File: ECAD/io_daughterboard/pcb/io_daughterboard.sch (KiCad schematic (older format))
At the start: 33 parts, among them P1 CONN_02X32, P2 CONN_02X32

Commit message: Annotated P2 pins.
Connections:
- net labels added: BTN_USER, BTN_~RESET, LCD_B5, LCD_DE, LCD_G2, LCD_G4, LCD_G5, LCD_PWM, LCD_R3, LCD_R6, LCD_VSYNC, N/C, NRST, PA0, PA1, PA2, PA3, PA4, PA5, PA6, PA7, PB0, PB1, PB10, PB11, PB12, PB13, PB14, PB15, PB2, PC0, PC1, PC2, PC3, PC4, PC5, PD10, PD11, PD12, PD13, PD14, PD15, PD8, PD9, PE10, PE11, PE12, PE13, PE14, PE15, PE7, PE8, PE9, PF10, PF11, PF12, PF13, PF14, PF15, PF6, PF7, PF8, PF9, PG0, PG1, PG2, PG3, PH0, PH1, SPI1_MOSI, SPI1_SCK, SPI5_MISO, SPI5_MOSI, SPI5_SCK, SPI_C_~CS
- wire segments 76 -> 136
- no-connect marks 30 -> 70
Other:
- moved on the sheet: P2

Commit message: Added pushbuttons and MIDI 5V interface.
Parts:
- removed SW? (x2): SW_PUSH, symbol SW_PUSH
- added C?: 10nF, symbol C
- added C?: 1µF, symbol C
- added C? (x2): 1nF, symbol C
- added R? (x2): 100, symbol R
- added R? (x2): 1M, symbol R
- added SW?: User Button, symbol Button
- added SW?: Reset Button, symbol Button
- added U? (x2): SN74LV1T34DCKR, symbol SN74LV1T34DCKR
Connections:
- net labels added: BTN_RESET, MIDI_RX_5V, MIDI_TX_5V, PWR_SENS
- wire segments 136 -> 204
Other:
- moved on the sheet: CON?, J?, P1, P2, P?, U?

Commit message: Capacitive touch connector.
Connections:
- net +3V3: now also J?.3 (Vdd), P2.1 (P1), P2.2 (P2); no longer P2.63 (P63), P2.64 (P64)
- net BTN_USER: now also P2.17 (P17); no longer P2.48 (P48)
- net BTN_~RESET: now also P2.11 (P11); no longer P2.54 (P54)
- net GND: now also J?.6 (GND), P2.12 (P12), P2.30 (P30), P2.63 (P63), P2.64 (P64); no longer P2.1 (P1), P2.2 (P2), P2.35 (P35), P2.53 (P53)
- net I²C3_SCL: now also J?.1 (SCL)
- net I²C3_SDA: now also J?.2 (SDA)
- net LCD_B5: now also P2.20 (P20); no longer P2.45 (P45)
- net LCD_DE: now also P2.8 (P8); no longer P2.57 (P57)
- net LCD_G2: now also P2.23 (P23); no longer P2.42 (P42)
- net LCD_G4: now also P2.47 (P47); no longer P2.18 (P18)
- net LCD_G5: now also P2.48 (P48); no longer P2.17 (P17)
- net LCD_PWM: now also P2.4 (P4); no longer P2.61 (P61)
- net LCD_R3: now also P2.27 (P27); no longer P2.38 (P38)
- net LCD_R6: now also P2.28 (P28); no longer P2.37 (P37)
- net LCD_VSYNC: now also P2.21 (P21); no longer P2.44 (P44)
- net N/C: now also P2.3 (P3); no longer P2.62 (P62)
- net PA1: now also P2.18 (P18); no longer P2.47 (P47)
- net PA2: now also P2.19 (P19); no longer P2.46 (P46)
- net PA5: now also P2.22 (P22); no longer P2.43 (P43)
- net PA7: now also P2.24 (P24); no longer P2.41 (P41)
- net PB12: now also P2.49 (P49); no longer P2.16 (P16)
- net PB13: now also P2.50 (P50); no longer P2.15 (P15)
- net PB14: now also P2.51 (P51); no longer P2.14 (P14)
- net PB15: now also P2.52 (P52); no longer P2.13 (P13)
- net PB2: now also P2.29 (P29); no longer P2.36 (P36)
- net PC0: now also P2.13 (P13); no longer P2.52 (P52)
- net PC1: now also P2.14 (P14); no longer P2.51 (P51)
- net PC2: now also P2.15 (P15); no longer P2.50 (P50)
- net PC3: now also P2.16 (P16); no longer P2.49 (P49)
- net PC4: now also P2.25 (P25); no longer P2.40 (P40)
- net PC5: now also P2.26 (P26); no longer P2.39 (P39)
- net PD10: now also P2.55 (P55); no longer P2.10 (P10)
- net PD11: now also P2.56 (P56); no longer P2.9 (P9)
- net PD12: now also P2.57 (P57); no longer P2.8 (P8)
- net PD13: now also P2.58 (P58); no longer P2.7 (P7)
- net PD14: now also P2.59 (P59); no longer P2.6 (P6)
- net PD15: now also P2.60 (P60); no longer P2.5 (P5)
- net PD8: now also P2.53 (P53); no longer P2.12 (P12)
- net PD9: now also P2.54 (P54); no longer P2.11 (P11)
- net PE10: now also P2.41 (P41); no longer P2.24 (P24)
- net PE11: now also P2.42 (P42); no longer P2.23 (P23)
- net PE12: now also P2.43 (P43); no longer P2.22 (P22)
- net PE13: now also P2.44 (P44); no longer P2.21 (P21)
- net PE14: now also P2.45 (P45); no longer P2.20 (P20)
- net PE15: now also P2.46 (P46); no longer P2.19 (P19)
- net PE7: now also P2.38 (P38); no longer P2.27 (P27)
- net PE8: now also P2.39 (P39); no longer P2.26 (P26)
- net PE9: now also P2.40 (P40); no longer P2.25 (P25)
- net PF11: now also P2.31 (P31); no longer P2.34 (P34)
- net PF12: now also P2.32 (P32); no longer P2.33 (P33)
- net PF13: now also P2.33 (P33); no longer P2.32 (P32)
- net PF14: now also P2.34 (P34); no longer P2.31 (P31)
- net PF15: now also P2.35 (P35); no longer P2.30 (P30)
- net PF7: now also P2.5 (P5); no longer P2.60 (P60)
- net PF8: now also P2.6 (P6); no longer P2.59 (P59)
- net PF9: now also P2.7 (P7); no longer P2.58 (P58)
- net PG0: now also P2.36 (P36); no longer P2.29 (P29)
- net PG1: now also P2.37 (P37); no longer P2.28 (P28)
- net PG2: now also P2.61 (P61); no longer P2.4 (P4)
- net PG3: now also P2.62 (P62); no longer P2.3 (P3)
- net PH0: now also P2.9 (P9); no longer P2.56 (P56)
- net PH1: now also P2.10 (P10); no longer P2.55 (P55)
- net BACKLIGHT_V: now reaches J?.2 (LEDA)
- net CTOUCH_WAKE: now reaches J?.4 (WAKE)
- net CTOUCH_INT: now reaches J?.5 (INT)
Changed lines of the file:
@@
 F 3 "" H 4950 5000 50  0000 C CNN
 	1    4950 5400
-	1    0    0    1
+	-1   0    0    -1
 $EndComp
 $Comp
@@
 	2400 1300 2200 1300
 Wire Wire Line
-	2200 1300 2200 1000
-Wire Wire Line
-	1450 1000 1550 1000
-Wire Wire Line
-	1550 1000 2200 1000
-Wire Wire Line
-	2200 1000 2400 1000
+	2200 1000 2200 1300
+Wire Wire Line
+	1450 1000 2400 1000
 Connection ~ 2200 1000
 Wire Wire Line
@@
 $EndComp
 Wire Wire Line
-	3300 1000 3650 1000
-Wire Wire Line
-	3650 1000 3750 1000
+	3300 1000 3750 1000
 Wire Wire Line
 	3650 1000 3650 1400
@@
 	3400 1300 3400 1400
 Wire Wire Line
-	1550 1000 1550 850
-Wire Wire Line
-	1550 850  1650 850
+	1550 1000 1550 900
+Wire Wire Line
+	1550 900  1650 900
 Connection ~ 1550 1000
 $Comp
 L +5V #PWR?
 U 1 1 58283D14
-P 1650 850
-F 0 "#PWR?" H 1650 700 50  0001 C CNN
-F 1 "+5V" H 1650 990 50  0000 C CNN
-F 2 "" H 1650 850 50  0000 C CNN
-F 3 "" H 1650 850 50  0000 C CNN
-	1    1650 850
+P 1650 900
+F 0 "#PWR?" H 1650 750 50  0001 C CNN
+F 1 "+5V" H 1650 1040 50  0000 C CNN
+F 2 "" H 1650 900 50  0000 C CNN
+F 3 "" H 1650 900 50  0000 C CNN
+	1    1650 900
 	0    1    1    0
 $EndComp
@@
 $EndComp
 Wire Wire Line
-	5450 950  5550 950
-Wire Wire Line
-	5550 950  5650 950
+	5450 950  5650 950
 Wire Wire Line
 	5550 1050 5450 1050
@@
 $EndComp
 Wire Wire Line
-	4500 1050 4750 1050
-Wire Wire Line
-	4750 1050 4850 1050
-Wire Wire Line
-	4750 950  4750 1050
-Wire Wire Line
-	4750 1050 4750 1150
-Wire Wire Line
-	4200 950  4750 950
-Wire Wire Line
-	4750 950  4850 950
+	4500 1050 4850 1050
+Wire Wire Line
+	4750 950  4750 1150
+Wire Wire Line
+	4200 950  4850 950
 Connection ~ 4750 950
 Wire Wire Line
@@
 	6050 2450 6050 3050
 Wire Wire Line
-	5450 2450 5550 2450
-Wire Wire Line
-	5550 2450 5650 2450
+	5450 2450 5650 2450
 Wire Wire Line
 	5450 2550 5550 2550
@@
 	4750 3050 4750 2950
 Wire Wire Line
-	4750 2350 4750 2450
-Wire Wire Line
-	4750 2450 4750 2550
-Wire Wire Line
-	4750 2550 4750 2650
-Wire Wire Line
-	4200 2450 4750 2450
-Wire Wire Line
-	4750 2450 4850 2450
+	4750 2350 4750 2650
+Wire Wire Line
+	4200 2450 4850 2450
 Connection ~ 4750 2450
 Wire Wire Line
@@
 	1    0    0    -1
 $EndComp
+Wire Wire Line
+	15550 1000 14850 1000
+Wire Wire Line
+	15550 1100 14850 1100
+Wire Wire Line
+	15550 1200 14850 1200
+Wire Wire Line
+	15550 1300 14850 1300
+Wire Wire Line
+	15550 1400 14850 1400
+Wire Wire Line
+	15550 1500 15450 1500
+Wire Wire Line
+	15450 1500 15450 1600
+$Comp
+L GND #PWR?
+U 1 1 58290783
+P 15450 1600
+F 0 "#PWR?" H 15450 1350 50  0001 C CNN
+F 1 "GND" H 15450 1450 50  0000 C CNN
+F 2 "" H 15450 1600 50  0000 C CNN
+F 3 "" H 15450 1600 50  0000 C CNN
+	1    15450 1600
+	1    0    0    -1
+$EndComp
+$Comp
+L +3.3V #PWR?
+U 1 1 5829086E
+P 14850 1200
+F 0 "#PWR?" H 14850 1050 50  0001 C CNN
+F 1 "+3.3V" V 14850 1450 50  0000 C CNN
+F 2 "" H 14850 1200 50  0000 C CNN
+F 3 "" H 14850 1200 50  0000 C CNN
+	1    14850 1200
+	0    -1   -1   0
+$EndComp
+Text Label 14850 1000 0    60   ~ 0
+I²C3_SCL
+Text Label 14850 1100 0    60   ~ 0
+I²C3_SDA
+Text Label 14850 1300 0    60   ~ 0
+CTOUCH_WAKE
+Text Label 14850 1400 0    60   ~ 0
+CTOUCH_INT
+Wire Wire Line
+	15550 2100 14850 2100
+Text Label 14850 2100 0    60   ~ 0
+BACKLIGHT_V
 $EndSCHEMATC

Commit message: Schematic: hooked up LCD connector.
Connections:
- net LCD_ON_OFF is gone; now on net LCD_DISP: P1.13 (P13)
- net +3V3: now also J?.4 (Vdd)
- net GND: now also J?.29 (GND), J?.3 (GND), J?.36 (GND)
- net LCD_B2: now also J?.23 (B2)
- net LCD_B3: now also J?.24 (B3)
- net LCD_B4: now also J?.25 (B4)
- net LCD_B5: now also J?.26 (B5)
- net LCD_B6: now also J?.27 (B6)
- net LCD_B7: now also J?.28 (B7)
- net LCD_CLK: now also J?.30 (CLK)
- net LCD_DE: now also J?.34 (DEN)
- net LCD_G2: now also J?.15 (G2)
- net LCD_G3: now also J?.16 (G3)
- net LCD_G4: now also J?.17 (G4)
- net LCD_G5: now also J?.18 (G5)
- net LCD_G6: now also J?.19 (G6)
- net LCD_G7: now also J?.20 (G7)
- net LCD_HSYNC: now also J?.32 (HSYNC)
- net LCD_R2: now also J?.7 (R2)
- net LCD_R3: now also J?.8 (R3)
- net LCD_R4: now also J?.9 (R4)
- net LCD_R5: now also J?.10 (R5)
- net LCD_R6: now also J?.11 (R6)
- net LCD_R7: now also J?.12 (R7)
- net LCD_VSYNC: now also J?.33 (VSYNC)
- net BKLT_K: now reaches J?.1 (LEDK)
- net LCD_G0: now reaches J?.13 (G0)
- net LCD_B0: now reaches J?.21 (B0)
- net LCD_B1: now reaches J?.22 (B1)
- net LCD_DISP: now reaches J?.31 (DISP)
- net RTOUCH_XR: now reaches J?.37 (XR)
- net RTOUCH_YD: now reaches J?.38 (YD)
- net RTOUCH_XL: now reaches J?.39 (XL)
- net RTOUCH_YU: now reaches J?.40 (YU)
- net LCD_R0: now reaches J?.5 (R0)
- net LCD_R1: now reaches J?.6 (R1)
- net LCD_G1: now reaches J?.G1 (14)
- net BACKLIGHT_V renamed BKLT_A

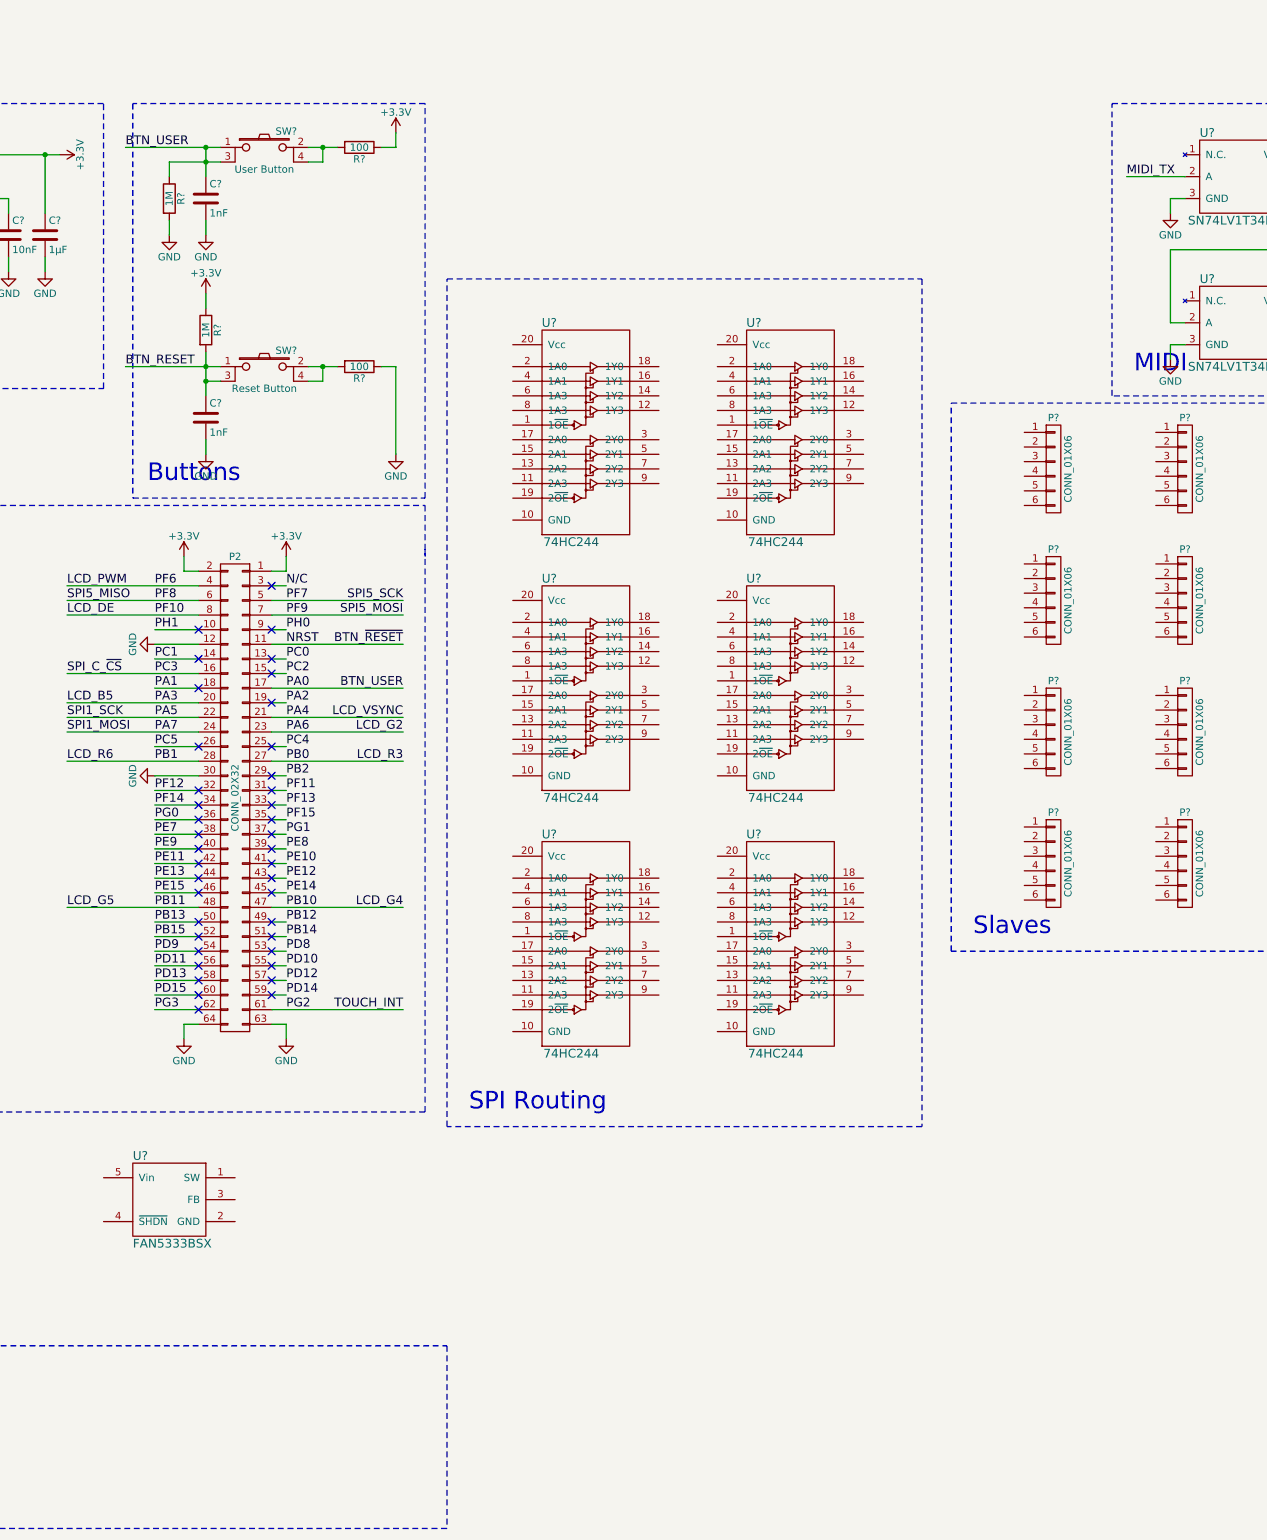
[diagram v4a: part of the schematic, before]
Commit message: Schematic for backlight power supply drawn.
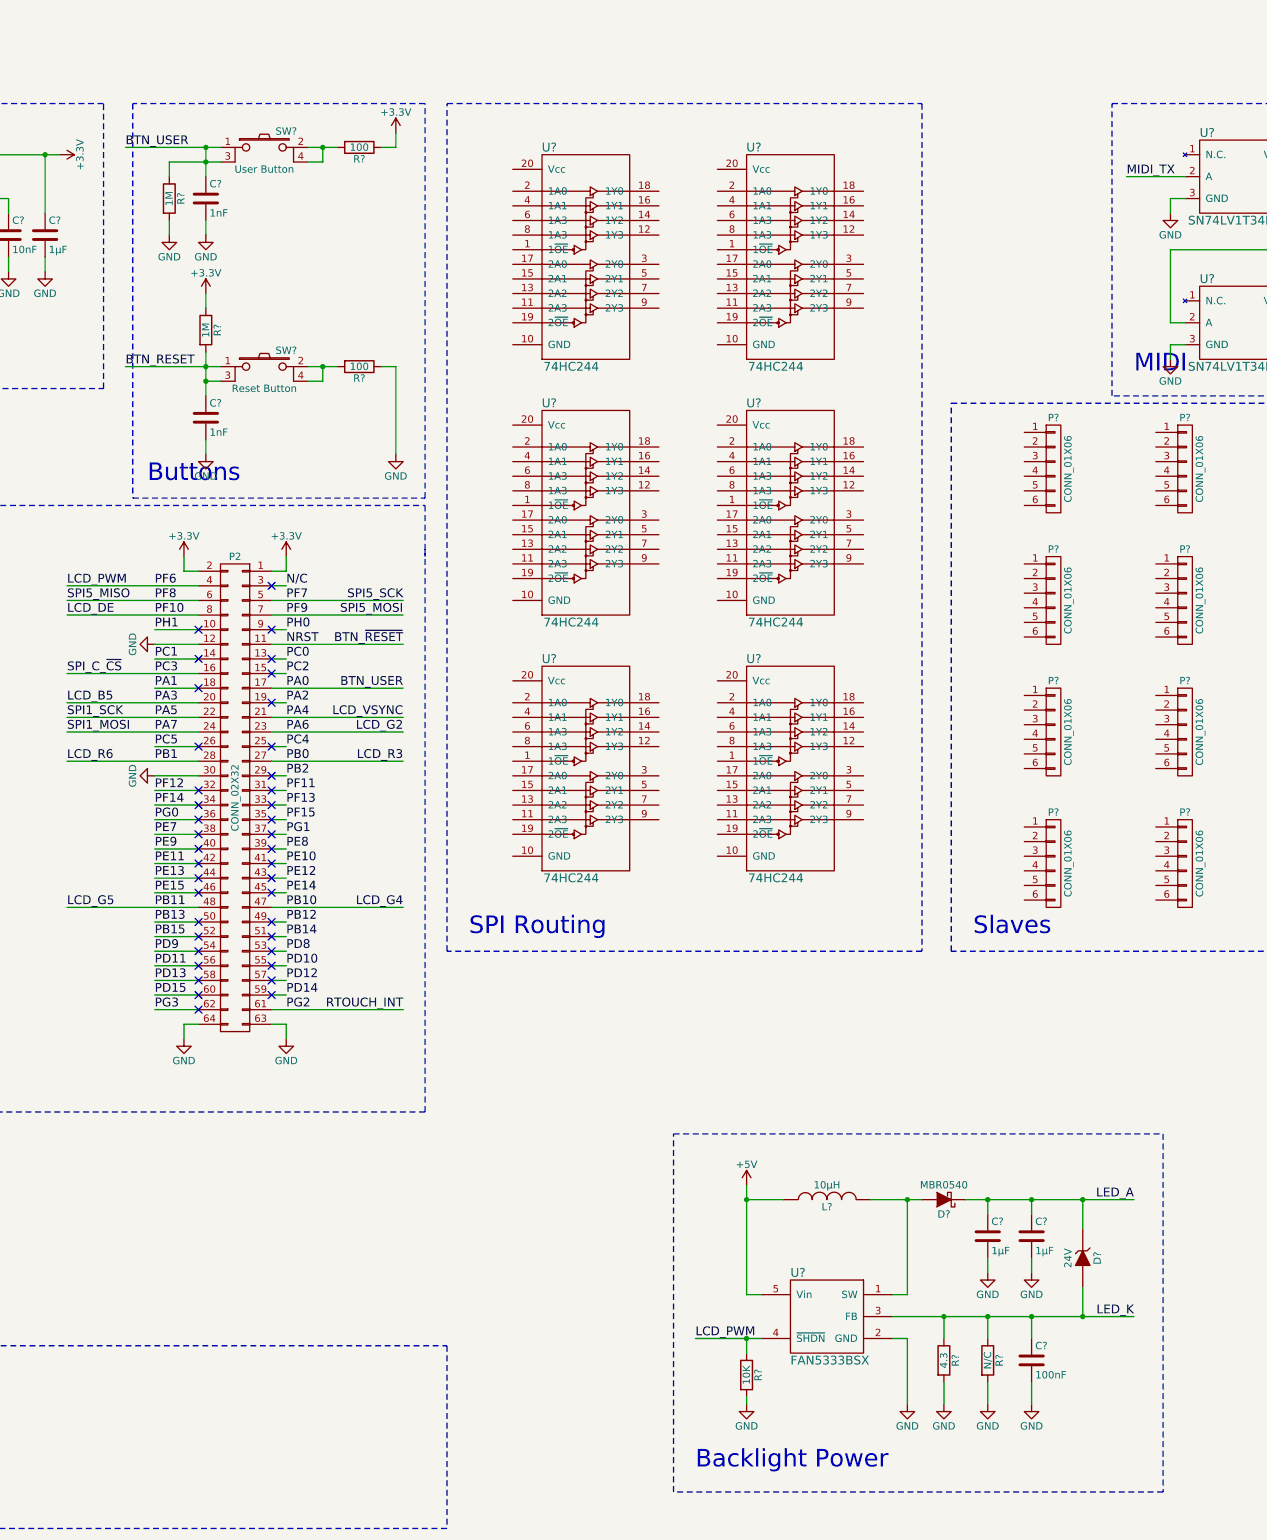
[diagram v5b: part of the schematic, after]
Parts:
- added C?: 100nF, symbol C
- added C? (x2): 1µF, symbol C
- added D?: MBR0540, symbol D_Schottky
- added D?: 24V, symbol ZENER
- added L?: 10µH, symbol INDUCTOR
- added R?: 4.3, symbol R
- added R?: N/C, symbol R
- added R?: 10K, symbol R
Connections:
- net +5V: now also U?.5 (Vin), L?.1
- net GND: now also U?.2 (GND), C?.2, C?.2, C?.2, R?.2, R?.2, R?.2
- net LCD_PWM: now also U?.4 (~SHDN), R?.1
- net at U?.1 (SW): now also D?.2 (A), L?.2
- net LED_K: now reaches U?.3 (FB)
- net LED_K: now also C?.1, D?.2 (A), R?.1, R?.1
- new net LED_A: C?.1, C?.1, D?.1 (K), D?.1 (K)
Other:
- note added: "Backlight Power"
- moved on the sheet: U?
